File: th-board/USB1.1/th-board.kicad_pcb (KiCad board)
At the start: 2 copper layers, 23.6 x 38.6 mm, 24 parts, among them J1 USB_A, J2 Conn_01x04, J3 Conn_01x02, U1 ESP-12F, U2 DHT11, U3 SPX3819M5-L

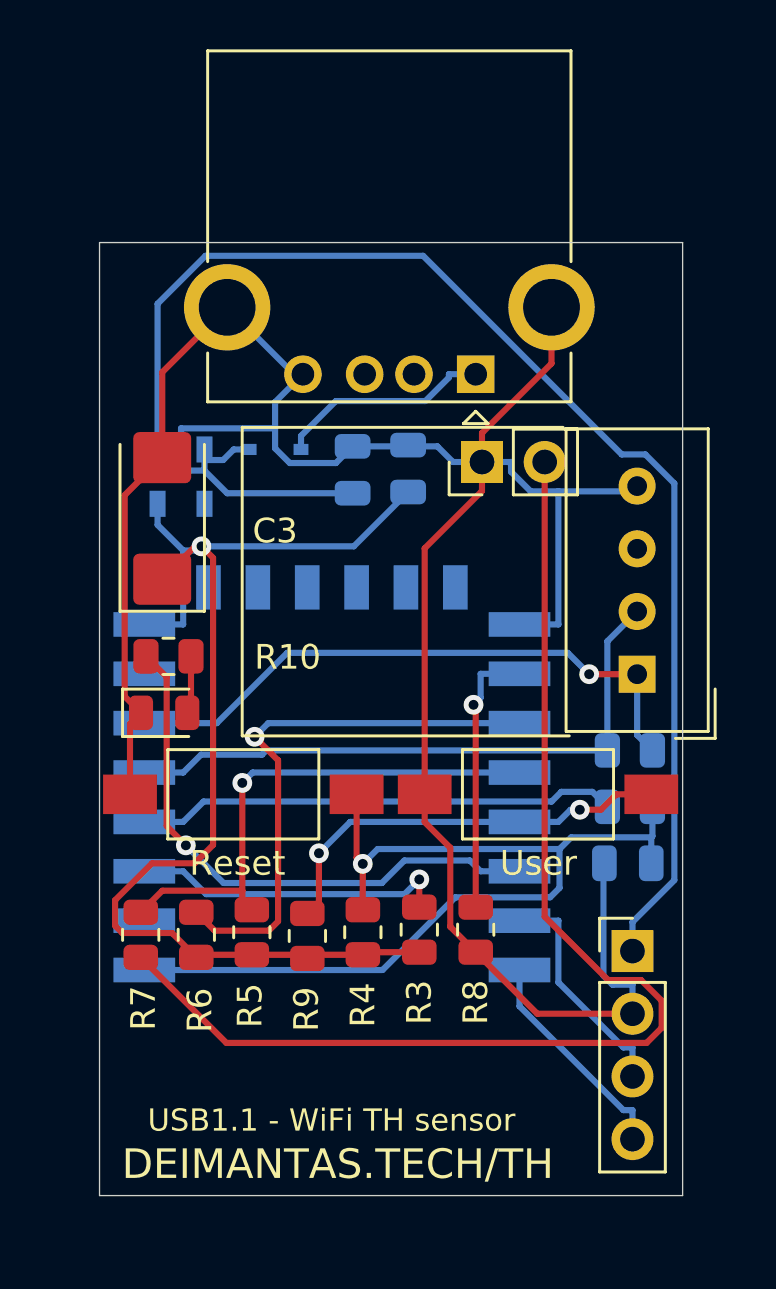
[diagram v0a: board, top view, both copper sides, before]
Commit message: PCB: add ground fill
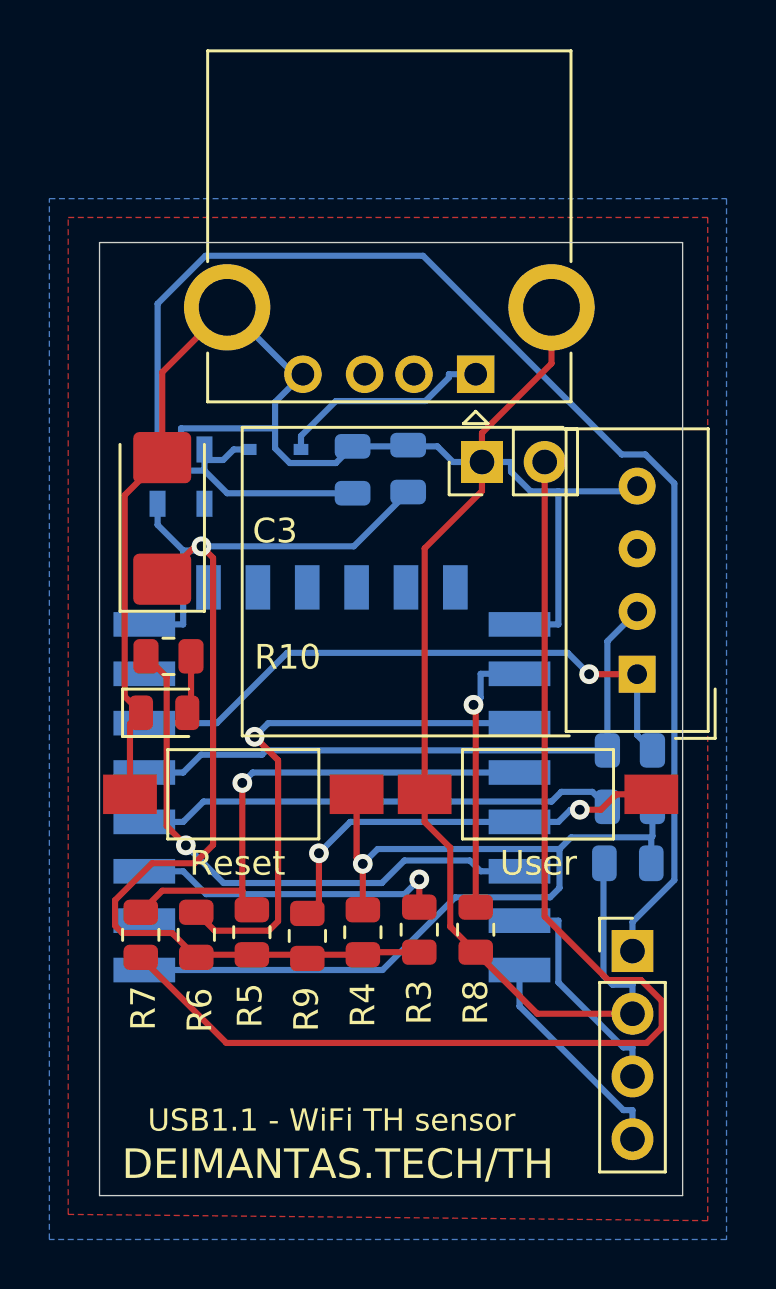
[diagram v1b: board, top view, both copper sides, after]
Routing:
- added copper zone on B.Cu, net USB_GND
- added copper zone on F.Cu, net USB_GND
